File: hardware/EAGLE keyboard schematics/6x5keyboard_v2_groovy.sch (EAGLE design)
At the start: 71 parts

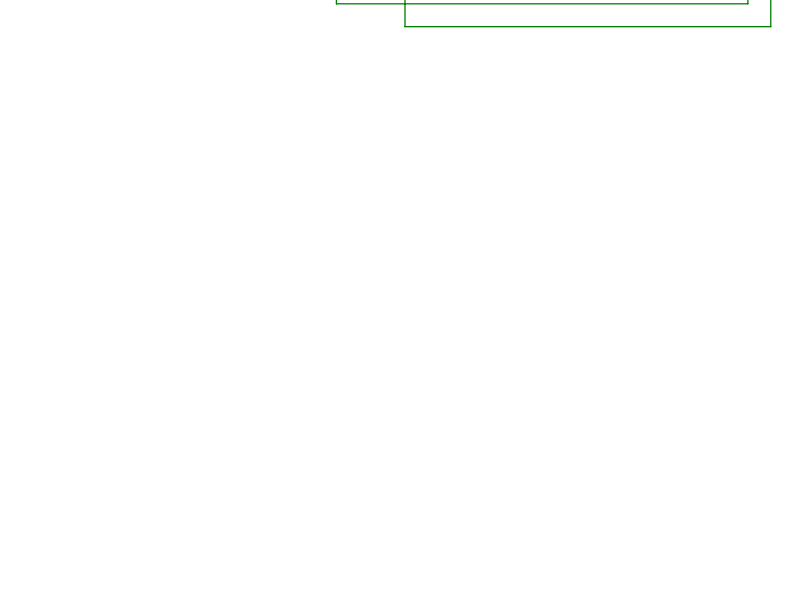
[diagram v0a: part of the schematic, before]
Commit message: Groovy traces now in their own files.  6x5keyboard_v2_untested.* is exclusively right-angle traces now.
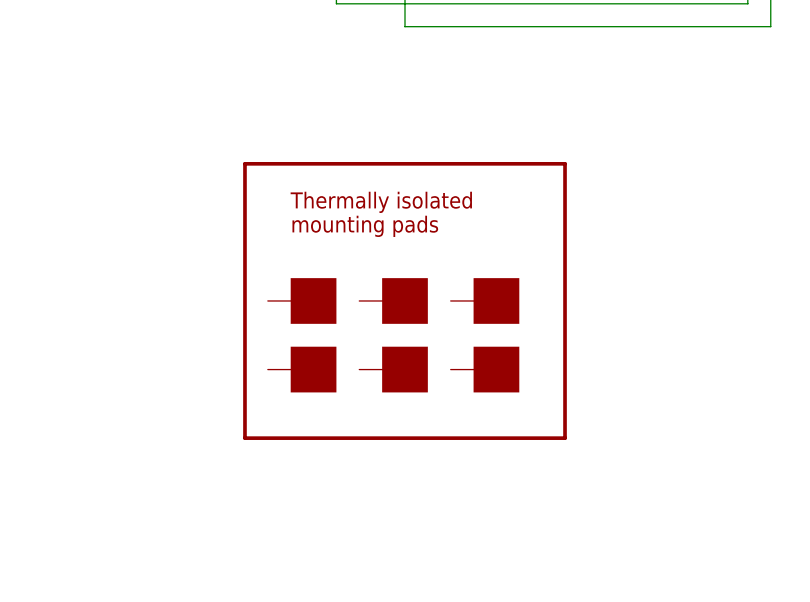
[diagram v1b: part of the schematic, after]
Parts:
- added U$36, U$37, U$38, U$39, U$40, U$41: MOUNTING-PAD, my_parts:MOUNTING-PAD
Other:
- note added: "Thermally isolated mounting pads"
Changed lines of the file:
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@@
 <part name="SUPPLY5" library="supply2" deviceset="GND" device=""/>
 <part name="P+1" library="supply1" deviceset="VCC" device=""/>
+<part name="U$36" library="my_parts" deviceset="MOUNTING-PAD" device=""/>
+<part name="U$37" library="my_parts" deviceset="MOUNTING-PAD" device=""/>
+<part name="U$38" library="my_parts" deviceset="MOUNTING-PAD" device=""/>
+<part name="U$39" library="my_parts" deviceset="MOUNTING-PAD" device=""/>
+<part name="U$40" library="my_parts" deviceset="MOUNTING-PAD" device=""/>
+<part name="U$41" library="my_parts" deviceset="MOUNTING-PAD" device=""/>
 </parts>
 <sheets>
 <sheet>
 <plain>
+<wire x1="-50.8" y1="45.72" x2="-15.24" y2="45.72" width="0.4064" layer="94"/>
+<wire x1="-15.24" y1="45.72" x2="-15.24" y2="15.24" width="0.4064" layer="94"/>
+<wire x1="-15.24" y1="15.24" x2="-50.8" y2="15.24" width="0.4064" layer="94"/>
+<wire x1="-50.8" y1="15.24" x2="-50.8" y2="45.72" width="0.4064" layer="94"/>
+<text x="-45.72" y="38.1" size="1.778" layer="94">Thermally isolated
+mounting pads</text>
 </plain>
 <instances>
@@
 <instance part="SUPPLY5" gate="GND" x="-71.12" y="93.98" rot="R90"/>
 <instance part="P+1" gate="VCC" x="-86.36" y="149.86"/>
+<instance part="U$36" gate="G$1" x="-43.18" y="30.48"/>
+<instance part="U$37" gate="G$1" x="-22.86" y="30.48"/>
+<instance part="U$38" gate="G$1" x="-33.02" y="30.48"/>
+<instance part="U$39" gate="G$1" x="-33.02" y="22.86"/>
+<instance part="U$40" gate="G$1" x="-43.18" y="22.86"/>
+<instance part="U$41" gate="G$1" x="-22.86" y="22.86"/>
 </instances>
 <busses>
